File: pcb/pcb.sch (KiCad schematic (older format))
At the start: 127 parts, among them J1 USB_C_Receptacle_USB2.0, J2 AVR-ISP-6, SW1 SW_Push, U1 ATmega32U4-AU, U2 PRTR5V0U2X, Y1 16MHz

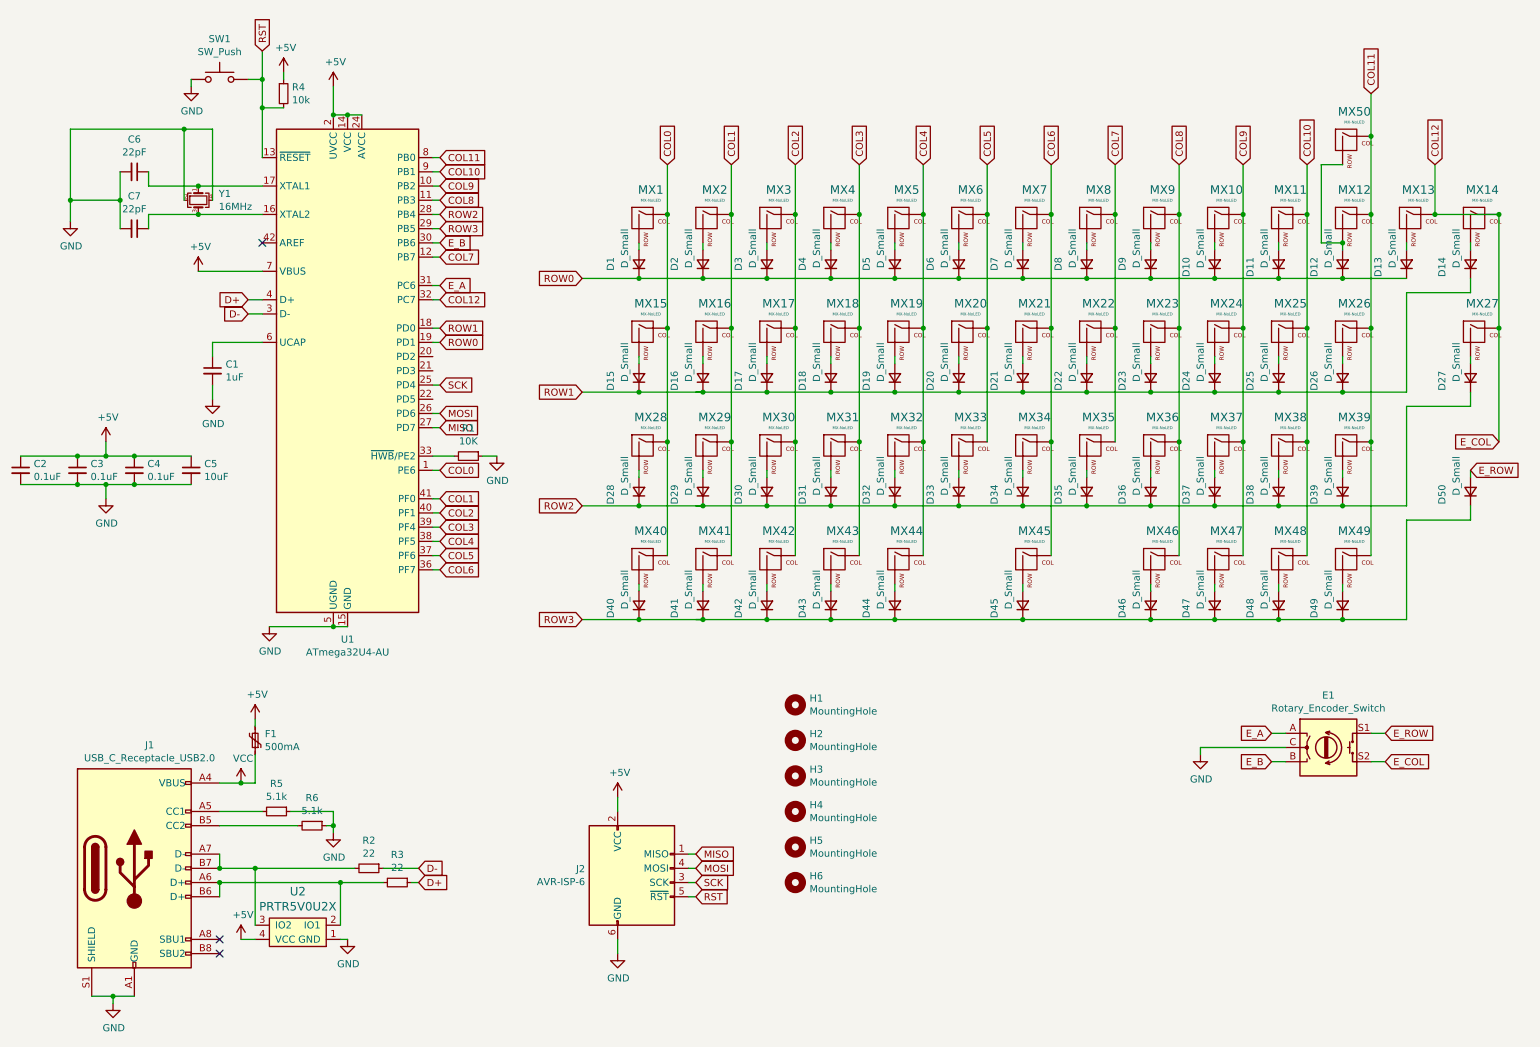
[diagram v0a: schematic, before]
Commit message: add LED and reshape width of macros spacer
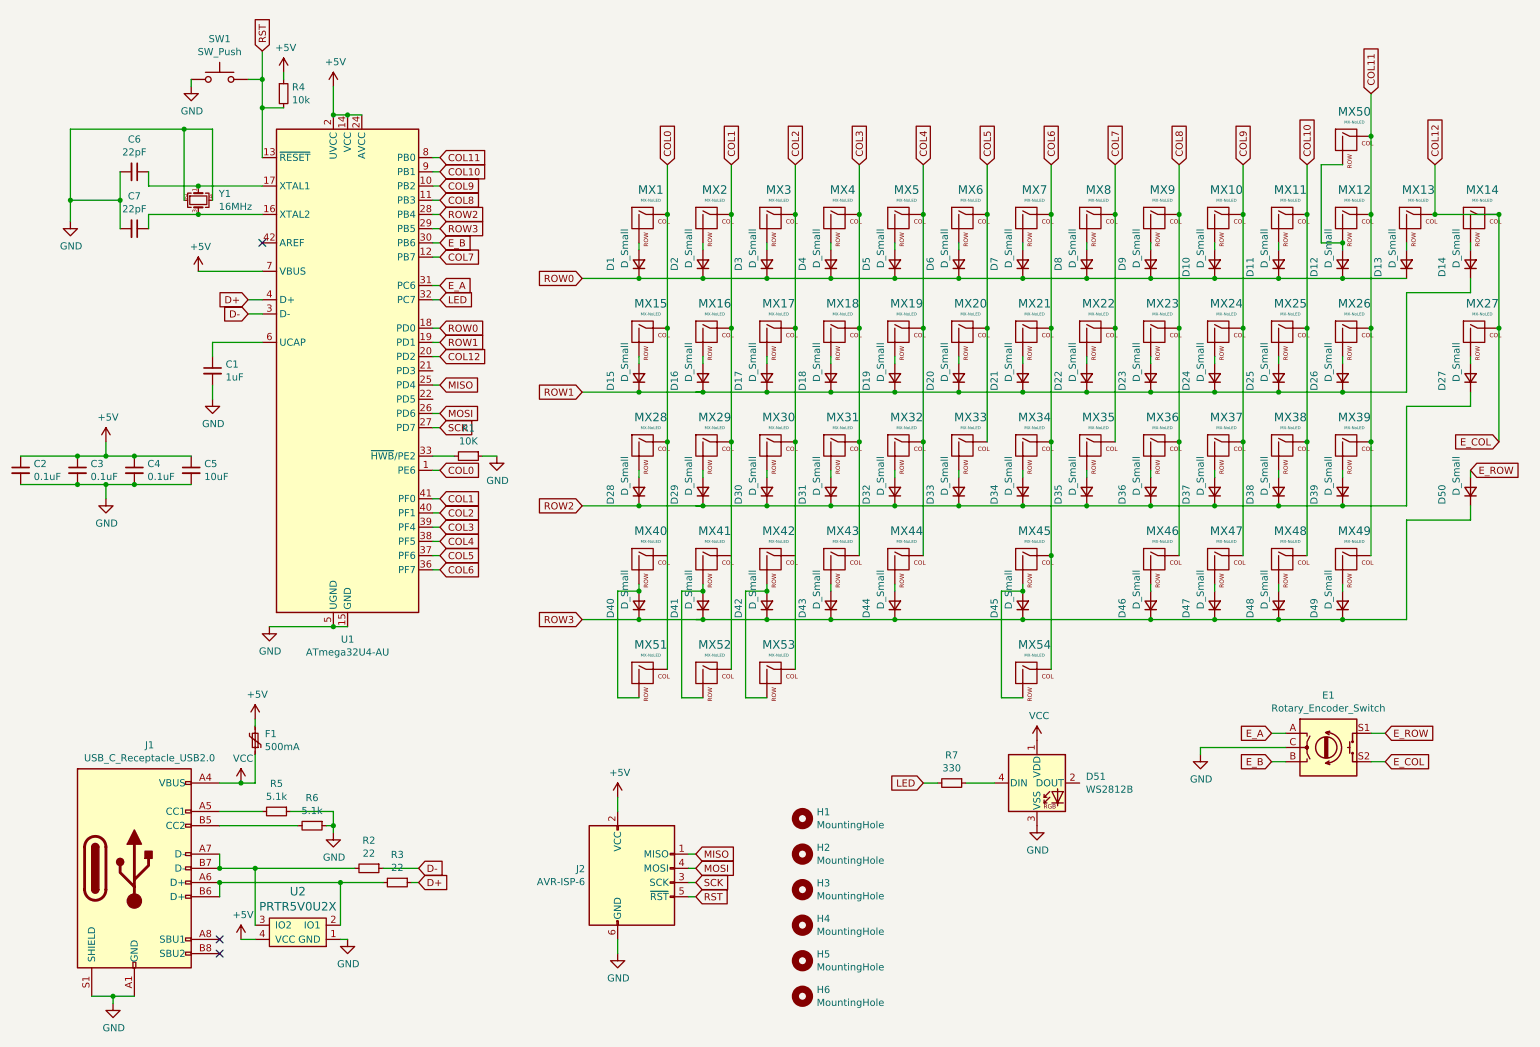
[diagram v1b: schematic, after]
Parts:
- added D51: WS2812B, LED_SMD:LED_WS2812B_PLCC4_5.0x5.0mm_P3.2mm, symbol LED:WS2812B
- added MX51, MX52, MX53: MX-NoLED, MX_Alps_Hybrid:MX-1.25U-NoLED, symbol MX_Alps_Hybrid:MX-NoLED
- added MX54: MX-NoLED, MX_Alps_Hybrid:MX-6U-Centered-ReversedStabilizers-NoLED, symbol MX_Alps_Hybrid:MX-NoLED
- added R7: 330, Resistor_SMD:R_0805_2012Metric, symbol Device:R_Small
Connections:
- net COL0: now also MX51.1 (COL)
- net COL1: now also MX52.1 (COL)
- net COL12: now also U1.20 (PD2); no longer U1.32 (PC7)
- net COL2: now also MX53.1 (COL)
- net COL6: now also MX54.1 (COL)
- net GND: now also D51.3 (VSS)
- net MISO: now also U1.25 (PD4); no longer U1.27 (PD7)
- net ROW0: now also U1.18 (PD0); no longer U1.19 (PD1)
- net ROW1: now also U1.19 (PD1); no longer U1.18 (PD0)
- net SCK: now also U1.27 (PD7); no longer U1.25 (PD4)
- net VCC: now also D51.1 (VDD)
- net at D40.2 (A), MX40.2 (ROW): now also MX51.2 (ROW)
- net at D41.2 (A), MX41.2 (ROW): now also MX52.2 (ROW)
- net at D42.2 (A), MX42.2 (ROW): now also MX53.2 (ROW)
- net at D45.2 (A), MX45.2 (ROW): now also MX54.2 (ROW)
- new net: D51.4 (DIN), R7.1
- new net LED: R7.2, U1.32 (PC7)
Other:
- moved on the sheet: H1, H2, H3, H4, H5, H6
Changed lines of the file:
@@
 	5000 3950 4600 3950
 Connection ~ 5000 3950
-Wire Wire Line
-	4600 4750 5000 4750
 Connection ~ 5000 4750
 Connection ~ 5450 4750
@@
 Text GLabel 3600 2100 2    50   Input ~ 0
 E_B
-Text GLabel 3600 2800 2    50   Input ~ 0
+Text GLabel 3600 2700 2    50   Input ~ 0
 ROW0
-Text GLabel 3600 3400 2    50   Input ~ 0
+Text GLabel 3600 3100 2    50   Input ~ 0
 MISO
 Wire Wire Line
@@
 Wire Wire Line
 	3600 2000 3550 2000
-Text GLabel 3600 3100 2    50   Input ~ 0
+Text GLabel 3600 3400 2    50   Input ~ 0
 SCK
 Text GLabel 4600 4750 0    50   Input ~ 0
@@
 Text GLabel 3600 1900 2    50   Input ~ 0
 ROW2
-Text GLabel 3600 2700 2    50   Input ~ 0
+Text GLabel 3600 2800 2    50   Input ~ 0
 ROW1
 Wire Wire Line
 	11050 3500 11050 2700
 Connection ~ 11050 2700
-Text GLabel 3600 2500 2    50   Input ~ 0
+Text GLabel 3600 2900 2    50   Input ~ 0
 COL12
 Wire Wire Line
@@
 L Mechanical:MountingHole H1
 U 1 1 61D66065
-P 6100 5350
-F 0 "H1" H 6200 5396 50  0000 L CNN
-F 1 "MountingHole" H 6200 5305 50  0000 L CNN
-F 2 "MountingHole:MountingHole_2.2mm_M2_Pad" H 6100 5350 50  0001 C CNN
-F 3 "~" H 6100 5350 50  0001 C CNN
-	1    6100 5350
+P 6150 6150
+F 0 "H1" H 6250 6196 50  0000 L CNN
+F 1 "MountingHole" H 6250 6105 50  0000 L CNN
+F 2 "MountingHole:MountingHole_2.2mm_M2_Pad" H 6150 6150 50  0001 C CNN
+F 3 "~" H 6150 6150 50  0001 C CNN
+	1    6150 6150
 	1    0    0    -1
 $EndComp
@@
 L Mechanical:MountingHole H2
 U 1 1 61D67684
-P 6100 5600
-F 0 "H2" H 6200 5646 50  0000 L CNN
-F 1 "MountingHole" H 6200 5555 50  0000 L CNN
-F 2 "MountingHole:MountingHole_2.2mm_M2_Pad" H 6100 5600 50  0001 C CNN
-F 3 "~" H 6100 5600 50  0001 C CNN
-	1    6100 5600
+P 6150 6400
+F 0 "H2" H 6250 6446 50  0000 L CNN
+F 1 "MountingHole" H 6250 6355 50  0000 L CNN
+F 2 "MountingHole:MountingHole_2.2mm_M2_Pad" H 6150 6400 50  0001 C CNN
+F 3 "~" H 6150 6400 50  0001 C CNN
+	1    6150 6400
 	1    0    0    -1
 $EndComp
@@
 L Mechanical:MountingHole H3
 U 1 1 61D6788A
-P 6100 5850
-F 0 "H3" H 6200 5896 50  0000 L CNN
-F 1 "MountingHole" H 6200 5805 50  0000 L CNN
-F 2 "MountingHole:MountingHole_2.2mm_M2_Pad" H 6100 5850 50  0001 C CNN
-F 3 "~" H 6100 5850 50  0001 C CNN
-	1    6100 5850
+P 6150 6650
+F 0 "H3" H 6250 6696 50  0000 L CNN
+F 1 "MountingHole" H 6250 6605 50  0000 L CNN
+F 2 "MountingHole:MountingHole_2.2mm_M2_Pad" H 6150 6650 50  0001 C CNN
+F 3 "~" H 6150 6650 50  0001 C CNN
+	1    6150 6650
 	1    0    0    -1
 $EndComp
@@
 L Mechanical:MountingHole H4
 U 1 1 61D67B2D
-P 6100 6100
-F 0 "H4" H 6200 6146 50  0000 L CNN
-F 1 "MountingHole" H 6200 6055 50  0000 L CNN
-F 2 "MountingHole:MountingHole_2.2mm_M2_Pad" H 6100 6100 50  0001 C CNN
-F 3 "~" H 6100 6100 50  0001 C CNN
-	1    6100 6100
+P 6150 6900
+F 0 "H4" H 6250 6946 50  0000 L CNN
+F 1 "MountingHole" H 6250 6855 50  0000 L CNN
+F 2 "MountingHole:MountingHole_2.2mm_M2_Pad" H 6150 6900 50  0001 C CNN
+F 3 "~" H 6150 6900 50  0001 C CNN
+	1    6150 6900
 	1    0    0    -1
 $EndComp
@@
 L Mechanical:MountingHole H5
 U 1 1 61D67CFA
-P 6100 6350
-F 0 "H5" H 6200 6396 50  0000 L CNN
-F 1 "MountingHole" H 6200 6305 50  0000 L CNN
-F 2 "MountingHole:MountingHole_2.2mm_M2_Pad" H 6100 6350 50  0001 C CNN
-F 3 "~" H 6100 6350 50  0001 C CNN
-	1    6100 6350
+P 6150 7150
+F 0 "H5" H 6250 7196 50  0000 L CNN
+F 1 "MountingHole" H 6250 7105 50  0000 L CNN
+F 2 "MountingHole:MountingHole_2.2mm_M2_Pad" H 6150 7150 50  0001 C CNN
+F 3 "~" H 6150 7150 50  0001 C CNN
+	1    6150 7150
 	1    0    0    -1
 $EndComp
@@
 L Mechanical:MountingHole H6
 U 1 1 61D67EAA
-P 6100 6600
-F 0 "H6" H 6200 6646 50  0000 L CNN
-F 1 "MountingHole" H 6200 6555 50  0000 L CNN
-F 2 "MountingHole:MountingHole_2.2mm_M2_Pad" H 6100 6600 50  0001 C CNN
-F 3 "~" H 6100 6600 50  0001 C CNN
-	1    6100 6600
+P 6150 7400
+F 0 "H6" H 6250 7446 50  0000 L CNN
+F 1 "MountingHole" H 6250 7355 50  0000 L CNN
+F 2 "MountingHole:MountingHole_2.2mm_M2_Pad" H 6150 7400 50  0001 C CNN
+F 3 "~" H 6150 7400 50  0001 C CNN
+	1    6150 7400
 	1    0    0    -1
 $EndComp
@@
 	1    0    0    -1
 $EndComp
+$Comp
+L MX_Alps_Hybrid:MX-NoLED MX51
+U 1 1 61DCA6CC
+P 5050 5150
+F 0 "MX51" H 5083 5373 60  0000 C CNN
+F 1 "MX-NoLED" H 5083 5299 20  0000 C CNN
+F 2 "MX_Alps_Hybrid:MX-1.25U-NoLED" H 4425 5125 60  0001 C CNN
+F 3 "" H 4425 5125 60  0001 C CNN
+	1    5050 5150
+	1    0    0    -1
+$EndComp
+$Comp
+L MX_Alps_Hybrid:MX-NoLED MX52
+U 1 1 61DCA6D9
+P 5500 5150
+F 0 "MX52" H 5533 5373 60  0000 C CNN
+F 1 "MX-NoLED" H 5533 5299 20  0000 C CNN
+F 2 "MX_Alps_Hybrid:MX-1.25U-NoLED" H 4875 5125 60  0001 C CNN
+F 3 "" H 4875 5125 60  0001 C CNN
+	1    5500 5150
+	1    0    0    -1
+$EndComp
+$Comp
+L MX_Alps_Hybrid:MX-NoLED MX53
+U 1 1 61DCA6E7
+P 5950 5150
+F 0 "MX53" H 5983 5373 60  0000 C CNN
+F 1 "MX-NoLED" H 5983 5299 20  0000 C CNN
+F 2 "MX_Alps_Hybrid:MX-1.25U-NoLED" H 5325 5125 60  0001 C CNN
+F 3 "" H 5325 5125 60  0001 C CNN
+	1    5950 5150
+	1    0    0    -1
+$EndComp
+Wire Wire Line
+	5200 4300 5200 5100
+Wire Wire Line
+	5650 4300 5650 5100
+Wire Wire Line
+	6100 4300 6100 5100
+Wire Wire Line
+	7900 5100 7900 4300
+$Comp
+L MX_Alps_Hybrid:MX-NoLED MX54
+U 1 1 61DCA718
+P 7750 5150
+F 0 "MX54" H 7783 5373 60  0000 C CNN
+F 1 "MX-NoLED" H 7783 5299 20  0000 C CNN
+F 2 "MX_Alps_Hybrid:MX-6U-Centered-ReversedStabilizers-NoLED" H 7125 5125 60  0001 C CNN
+F 3 "" H 7125 5125 60  0001 C CNN
+	1    7750 5150
+	1    0    0    -1
+$EndComp
+Connection ~ 7900 4300
+$Comp
+L LED:WS2812B D51
+U 1 1 61F8899F
+P 7800 5900
+F 0 "D51" H 8144 5946 50  0000 L CNN
+F 1 "WS2812B" H 8144 5855 50  0000 L CNN
+F 2 "LED_SMD:LED_WS2812B_PLCC4_5.0x5.0mm_P3.2mm" H 7850 5600 50  0001 L TNN
+F 3 "https://cdn-shop.adafruit.com/datasheets/WS2812B.pdf" H 7900 5525 50  0001 L TNN
+	1    7800 5900
+	1    0    0    -1
+$EndComp
+$Comp
+L power:VCC #PWR0120
+U 1 1 61F8C8E9
+P 7800 5600
+F 0 "#PWR0120" H 7800 5450 50  0001 C CNN
+F 1 "VCC" H 7815 5773 50  0000 C CNN
+F 2 "" H 7800 5600 50  0001 C CNN
+F 3 "" H 7800 5600 50  0001 C CNN
+	1    7800 5600
+	1    0    0    -1
+$EndComp
+$Comp
+L power:GND #PWR0121
+U 1 1 61F8E1F4
+P 7800 6200
+F 0 "#PWR0121" H 7800 5950 50  0001 C CNN
+F 1 "GND" H 7805 6027 50  0000 C CNN
+F 2 "" H 7800 6200 50  0001 C CNN
+F 3 "" H 7800 6200 50  0001 C CNN
+	1    7800 6200
+	1    0    0    -1
+$EndComp
+Wire Wire Line
+	4600 4750 5000 4750
+Wire Wire Line
+	5000 4550 4850 4550
+Wire Wire Line
+	4850 4550 4850 5300
+Wire Wire Line
+	4850 5300 5000 5300
+Connection ~ 5000 4550
+Wire Wire Line
+	5450 4550 5300 4550
+Wire Wire Line
+	5300 4550 5300 5300
+Wire Wire Line
+	5300 5300 5450 5300
+Connection ~ 5450 4550
+Wire Wire Line
+	5900 4550 5750 4550
+Wire Wire Line
+	5750 4550 5750 5300
+Wire Wire Line
+	5750 5300 5900 5300
+Connection ~ 5900 4550
+Wire Wire Line
+	7700 4550 7550 4550
+Wire Wire Line
+	7550 4550 7550 5300
+Wire Wire Line
+	7550 5300 7700 5300
+Connection ~ 7700 4550
+$Comp
+L Device:R_Small R7
+U 1 1 6211A7E3
+P 7200 5900
+F 0 "R7" V 7004 5900 50  0000 C CNN
+F 1 "330" V 7095 5900 50  0000 C CNN
+F 2 "Resistor_SMD:R_0805_2012Metric" H 7200 5900 50  0001 C CNN
+F 3 "~" H 7200 5900 50  0001 C CNN
+	1    7200 5900
+	0    1    1    0
+$EndComp
+Wire Wire Line
+	7500 5900 7300 5900
+Text GLabel 7000 5900 0    50   Input ~ 0
+LED
+Wire Wire Line
+	7100 5900 7000 5900
+Wire Wire Line
+	3600 2900 3550 2900
+Text GLabel 3600 2500 2    50   Input ~ 0
+LED
 $EndSCHEMATC

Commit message: create readme
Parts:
- renumbered D51 to LED1
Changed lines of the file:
@@
 Connection ~ 7900 4300
-$Comp
-L LED:WS2812B D51
-U 1 1 61F8899F
-P 7800 5900
-F 0 "D51" H 8144 5946 50  0000 L CNN
-F 1 "WS2812B" H 8144 5855 50  0000 L CNN
-F 2 "LED_SMD:LED_WS2812B_PLCC4_5.0x5.0mm_P3.2mm" H 7850 5600 50  0001 L TNN
-F 3 "https://cdn-shop.adafruit.com/datasheets/WS2812B.pdf" H 7900 5525 50  0001 L TNN
-	1    7800 5900
-	1    0    0    -1
-$EndComp
 $Comp
 L power:VCC #PWR0120
@@
 Text GLabel 3600 2500 2    50   Input ~ 0
 LED
+$Comp
+L LED:WS2812B LED1
+U 1 1 61F8899F
+P 7800 5900
+F 0 "LED1" H 8144 5946 50  0000 L CNN
+F 1 "WS2812B" H 8144 5855 50  0000 L CNN
+F 2 "LED_SMD:LED_WS2812B_PLCC4_5.0x5.0mm_P3.2mm" H 7850 5600 50  0001 L TNN
+F 3 "https://cdn-shop.adafruit.com/datasheets/WS2812B.pdf" H 7900 5525 50  0001 L TNN
+	1    7800 5900
+	1    0    0    -1
+$EndComp
 $EndSCHEMATC
